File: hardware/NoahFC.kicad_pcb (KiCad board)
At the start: 2 copper layers, 32 x 42 mm, 47 parts, among them J1 ALE, J10 ESC-, J11 CAM, J12 VTX, J13 ESC_GND, J14 ESC_PWM, J15 BEC+, J16 BEC-, J2 ELE, J3 VCC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

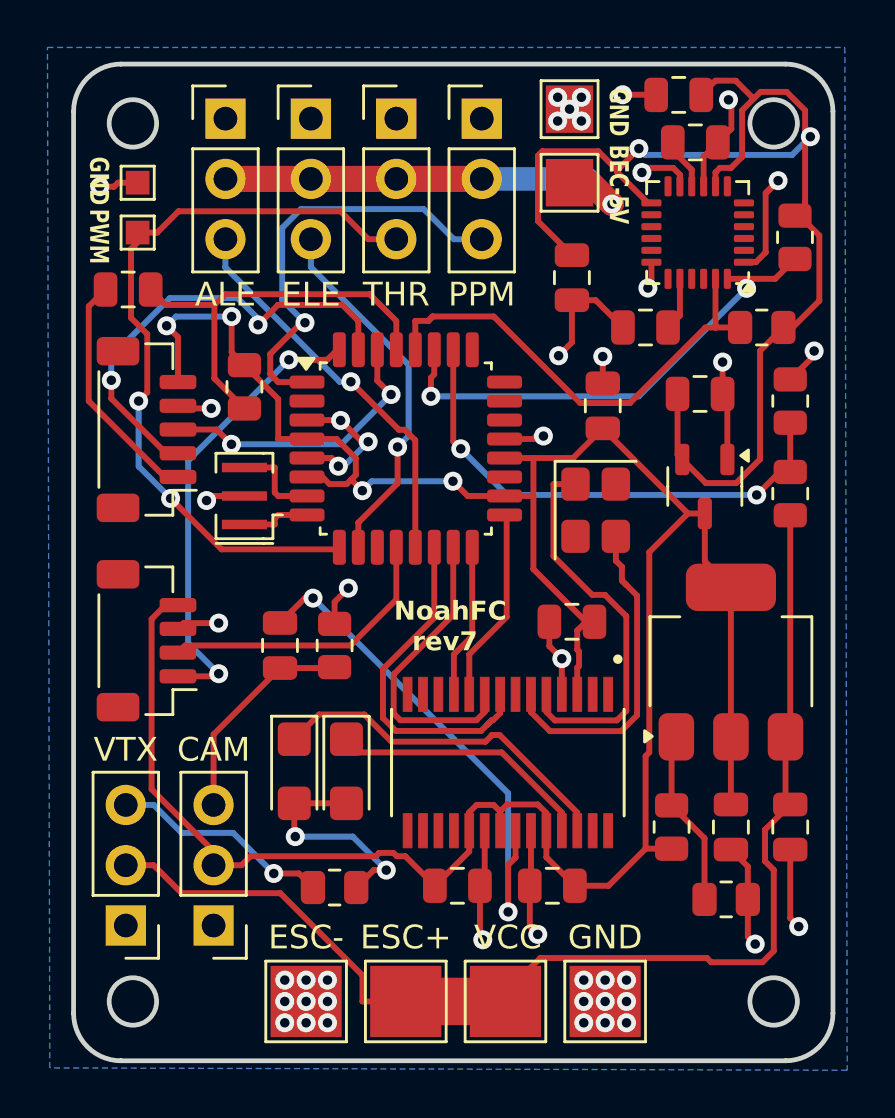
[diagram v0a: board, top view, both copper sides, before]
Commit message: update project with LCSC parts, fix some component prepare rev8
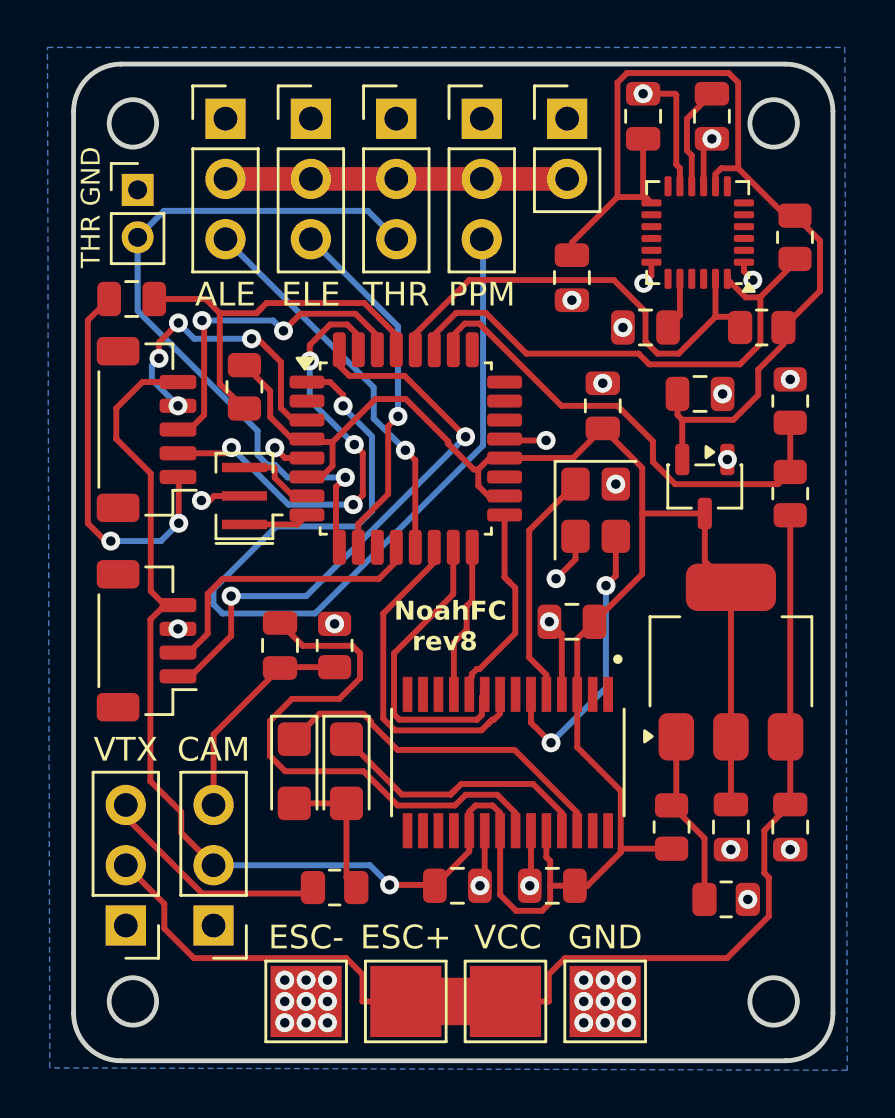
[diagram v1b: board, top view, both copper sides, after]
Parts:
- removed J13: ESC_GND, TestPoint:TestPoint_Pad_1.0x1.0mm
- removed J14: ESC_PWM, TestPoint:TestPoint_Pad_1.0x1.0mm
- removed J16: BEC-, TestPoint:TestPoint_Pad_2.0x2.0mm
- added J17: BEC, Connector_PinHeader_2.54mm:PinHeader_1x02_P2.54mm_Vertical, F.Cu at (83.0, 75.5)
- J15: value BEC+ -> ESC_PWM; footprint TestPoint:TestPoint_Pad_2.0x2.0mm -> Connector_PinHeader_2.00mm:PinHeader_1x02_P2.00mm_Vertical
- U3: value XC6206P332MR -> XC6206
- U4: value LM317_SOT-223 -> LM317
- U6: value MAX7456EUI+ -> AT7456
- moved J15 18.2 mm to (64.9, 78.5)
- moved C6 1.75 mm to (86.2, 75.4), turned to 90 degrees
- moved C8 1.30 mm to (89.1, 75.4), turned to -90 degrees
- moved C3 0.43 mm to (64.7, 83.1)
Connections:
- J15 pad 1: BEC_5V -> GND
- U6 pad 12: (no net) -> unconnected-(U6-LOS-Pad12)
- U6 pad 17: (no net) -> unconnected-(U6-~{VSYNC}-Pad17)
- U6 pad 18: (no net) -> unconnected-(U6-~{HSYNC}-Pad18)
- U6 pad 7: (no net) -> unconnected-(U6-CLKOUT-Pad7)
- Y3 pad 2: unconnected-(Y3-Pad2) -> GND
- Y3 pad 4: unconnected-(Y3-Pad4) -> GND
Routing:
- net GND: track 63.5 -> 37.8 mm, vias 46 -> 45
- net PPM: track 18.1 -> 39.9 mm
- net 3.3V: track 53.7 -> 41.4 mm, vias 2 -> 0
- net BEC_5V: track 26.4 -> 14.4 mm, vias 1 -> 0
- net XTAL1_OSD: track 16.5 -> 9.97 mm
- net DTR: track 10.1 -> 16.2 mm, vias 0 -> 2
- net GPS_RX: track 19.6 -> 24.5 mm
- net Net-(C18-Pad2): track 9.61 -> 5.92 mm, vias 2 -> 0
- net Net-(U2-REGOUT): track 2.18 -> 4.42 mm
- net RX: track 12.3 -> 14.2 mm
- net THROTTLE: track 32.2 -> 30.4 mm, vias 2 -> 1
- net XTAL2_OSD: track 14.0 -> 12.2 mm, vias 0 -> 2
- net VIN: track 22.0 -> 23.4 mm, vias 2 -> 0
- net SDA: track 20.9 -> 21.9 mm, vias 2 -> 0
- net VOLTAGE: track 21.6 -> 20.6 mm, vias 2 -> 0
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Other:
- board text added: "NoahFC rev8"
- board text added: "THR GND"
- board text removed: "BEC-5V"
- board text removed: "GND"
- board text removed: "NoahFC rev7"
- board text removed: "PWM"

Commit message: added 5V jumper for BEC
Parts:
- added REF**: PinHeader_1x01_P1.00mm_Vertical, Connector_PinHeader_1.00mm:PinHeader_1x01_P1.00mm_Vertical, F.Cu at (80.2, 97.8)
- added REF**: PinHeader_1x01_P1.00mm_Vertical, Connector_PinHeader_1.00mm:PinHeader_1x01_P1.00mm_Vertical, F.Cu at (67.5, 94.0)
- added REF**: PinHeader_1x01_P1.00mm_Vertical, Connector_PinHeader_1.00mm:PinHeader_1x01_P1.00mm_Vertical, F.Cu at (87.3, 93.2)
- added REF**: SolderJumper-2_P1.3mm_Open_RoundedPad1.0x1.5mm, Jumper:SolderJumper-2_P1.3mm_Open_RoundedPad1.0x1.5mm, F.Cu at (89.1, 112.9)
- added REF**: PinHeader_1x01_P1.00mm_Vertical, Connector_PinHeader_1.00mm:PinHeader_1x01_P1.00mm_Vertical, F.Cu at (66.9, 82.9)
- added REF**: PinHeader_1x01_P1.00mm_Vertical, Connector_PinHeader_1.00mm:PinHeader_1x01_P1.00mm_Vertical, F.Cu at (79.0, 95.2)
- added REF**: PinHeader_1x01_P1.00mm_Vertical, Connector_PinHeader_1.00mm:PinHeader_1x01_P1.00mm_Vertical, F.Cu at (76.1, 97.7)
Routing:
- net BEC_5V: track 14.4 -> 88.3 mm, vias 0 -> 2
- net 5V: track 114.7 -> 122.5 mm, vias 1 -> 3

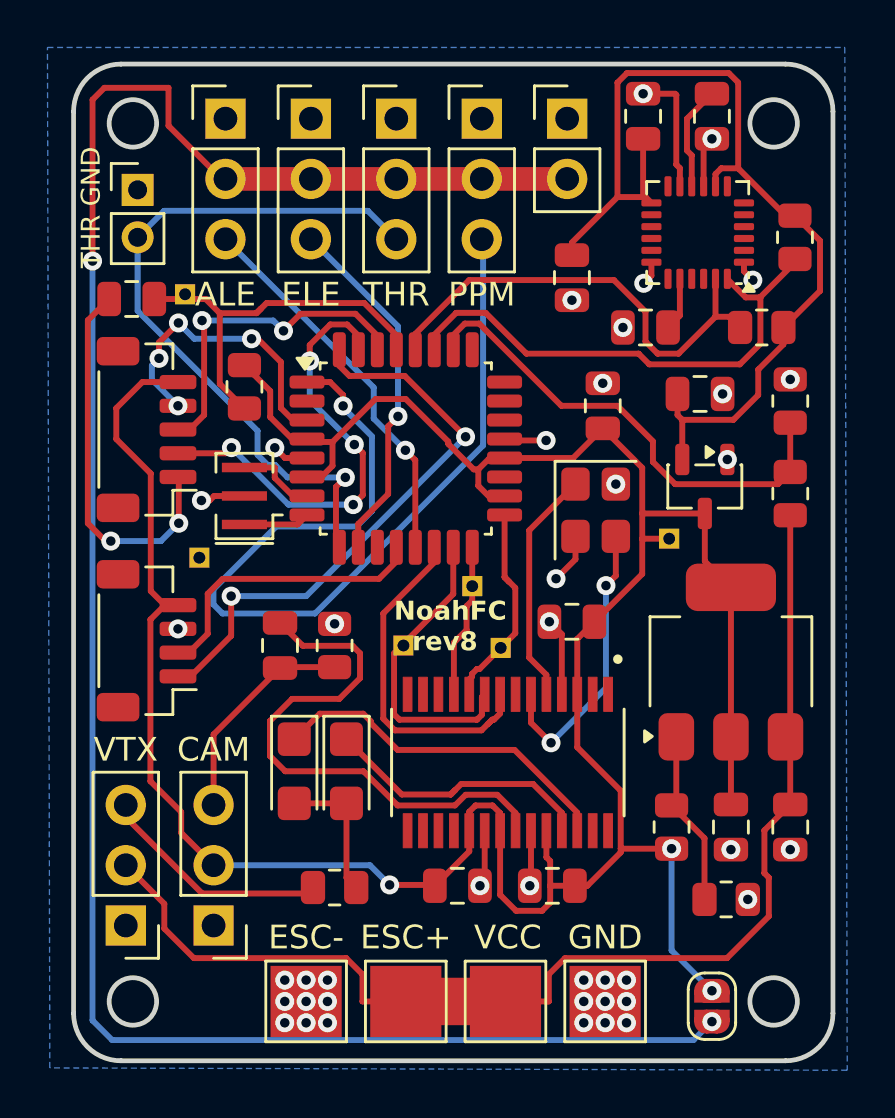
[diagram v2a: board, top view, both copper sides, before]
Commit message: add jumpers for vtx
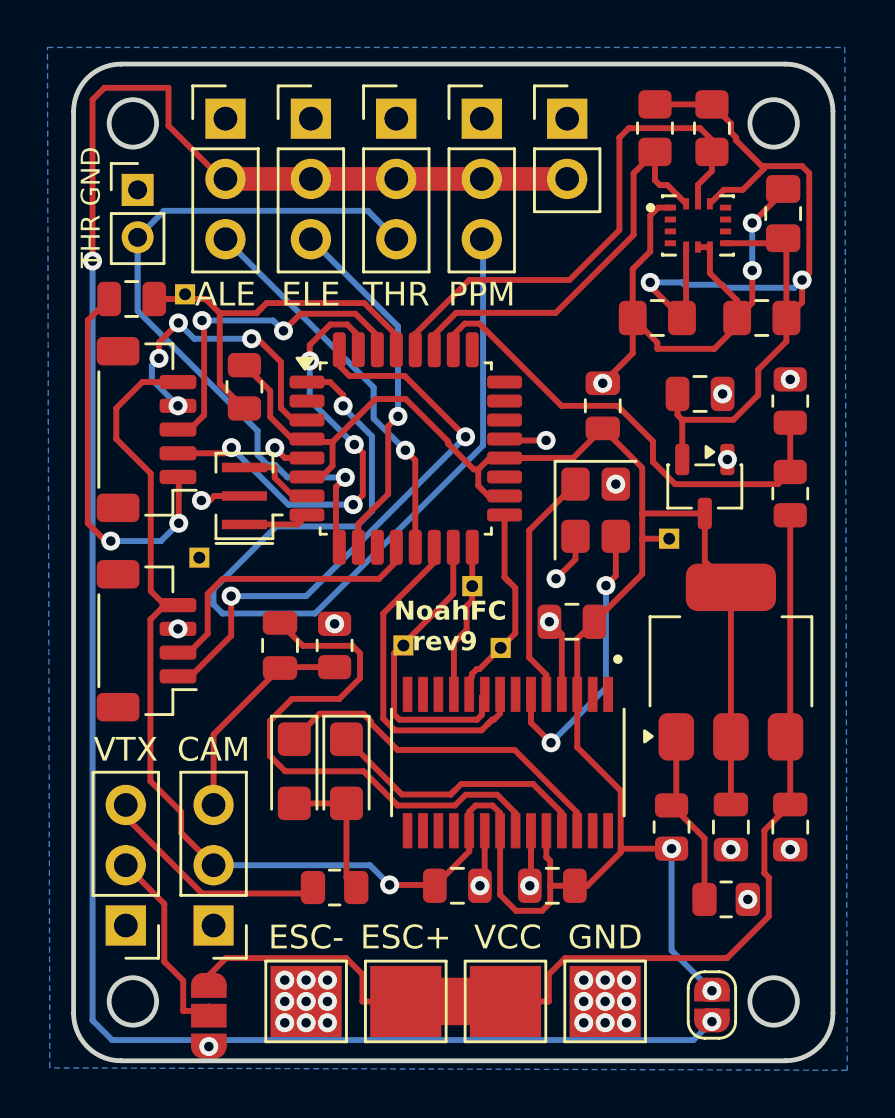
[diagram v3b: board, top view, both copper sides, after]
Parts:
- removed C6: 10nF, Capacitor_SMD:C_0805_2012Metric
- removed C7, C8: 100nF, Capacitor_SMD:C_0805_2012Metric
- removed C9: 2.2nF, Capacitor_SMD:C_0805_2012Metric
- removed R7, R8: 4.7K, Resistor_SMD:R_0805_2012Metric
- removed the REF** at (89.1, 112.9)
- removed U2: MPU-6050, Sensor_Motion:InvenSense_QFN-24_4x4mm_P0.5mm
- added C13: 100nF, Capacitor_SMD:C_0805_2012Metric_Pad1.18x1.45mm_HandSolder, F.Cu at (91.2, 83.9)
- added C14: 10nF, Capacitor_SMD:C_0805_2012Metric_Pad1.18x1.45mm_HandSolder, F.Cu at (86.8, 83.9)
- added C15: 2.2uF, Capacitor_SMD:C_0805_2012Metric_Pad1.18x1.45mm_HandSolder, F.Cu at (92.1, 79.5)
- added JP1: Jumper_3_Open, Jumper:SolderJumper-3_P1.3mm_Open_RoundedPad1.0x1.5mm, F.Cu at (67.9, 113.3)
- added JP2: Jumper_2_Open, Jumper:SolderJumper-2_P1.3mm_Open_RoundedPad1.0x1.5mm, F.Cu at (89.1, 112.8)
- added MT1: ICM-42670-P, ICM:XDCR_ICM-42670-P, F.Cu at (88.5, 80.0)
- added R3: 10K, Resistor_SMD:R_0805_2012Metric_Pad1.20x1.40mm_HandSolder, F.Cu at (89.1, 75.9)
- added R6: 10K, Resistor_SMD:R_0805_2012Metric_Pad1.20x1.40mm_HandSolder, F.Cu at (86.7, 75.9)
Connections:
- J12 pad 2: VCC -> VCC_VTX
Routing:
- net GND: track 37.8 -> 53.2 mm, vias 45 -> 41
- net VCC_VTX: track 0.00 -> 8.31 mm
- net VCC: track 50.5 -> 45.5 mm
- net Net-(U2-REGOUT): track 4.42 -> 0.00 mm
- net SDA: track 21.9 -> 17.6 mm
- net 3.3V: track 41.4 -> 45.4 mm, vias 0 -> 2
- net SCL: track 19.7 -> 22.2 mm
- net Net-(U2-CPOUT): track 2.26 -> 0.00 mm
- net BEC_5V: track 88.3 -> 88.6 mm, vias 2 -> 3
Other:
- board text added: "NoahFC rev9"
- board text removed: "NoahFC rev8"
